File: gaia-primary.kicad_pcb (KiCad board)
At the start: 4 copper layers, 50 x 50 mm, 24 parts, among them J1 4G antenna connector(U.FL), J6 Global Connector Technology S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, Q1 DTC143ZEBTL, Q3 DTC143ZEBTL, Q4 DTC143ZEBTL, U1 SIM7600E-H, U2 Gaia Connector A, U3 Gaia Connector B

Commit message: adding components
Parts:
- removed C18, C51: 1uF, Capacitor_SMD:C_1812_4532Metric
- removed C2, C20, C24, C4: 220uF, Capacitor_SMD:CP_Elec_5x5.9
- removed C3: 100nF, Capacitor_SMD:C_0402_1005Metric
- removed C47: 100nF, Capacitor_SMD:C_0603_1608Metric
- removed C49, C50: NM_NC, Capacitor_SMD:C_0402_1005Metric
- removed D1, D2: LED, LED_SMD:LED_0402_1005Metric
- removed J1: 4G antenna connector(U.FL), Connector_Coaxial:U.FL_Hirose_U.FL-R-SMT-1_Vertical
- removed J6: Global Connector Technology SIM8060-6-0-14-00-A, Connector_Card:nanoSIM_GCT_SIM8060-6-0-14-00
- removed Q1, Q3, Q4: DTC143ZEBTL, gaia-4gmodul-footprints:DTC143ZEBTL
- removed R19: 0, Resistor_SMD:R_0402_1005Metric
- removed R20: 0, Resistor_SMD:R_0603_1608Metric
- added C10: 10nF, Capacitor_SMD:C_0603_1608Metric, F.Cu at (130.0, 64.9)
- added C11: 100nF, Capacitor_SMD:C_0603_1608Metric, F.Cu at (130.0, 67.4)
- added C12: 100nF, Capacitor_SMD:C_0603_1608Metric, F.Cu at (130.0, 69.9)
- added C13: 10nF, Capacitor_SMD:C_0603_1608Metric, F.Cu at (130.0, 72.4)
- added C8: 100nF, Capacitor_SMD:C_0603_1608Metric, F.Cu at (130.0, 59.8)
- added C9: 100nF, Capacitor_SMD:C_0603_1608Metric, F.Cu at (130.0, 62.4)
- added U4: STM32F103C8Tx, Package_QFP:LQFP-48_7x7mm_P0.5mm, F.Cu at (189.4, 107.9)
- added U5: ICM-20948, Sensor_Motion:InvenSense_QFN-24_3x3mm_P0.4mm, F.Cu at (196.1, 75.0)
- added U6: BME680/BME690, Package_LGA:Bosch_LGA-8_3x3mm_P0.8mm_ClockwisePinNumbering, F.Cu at (207.2, 74.0)
- added U7: ICM-20948, Sensor_Motion:InvenSense_QFN-24_3x3mm_P0.4mm, F.Cu at (181.7, 75.1)
- added U8: MAX31865xTP, Package_DFN_QFN:TQFN-20-1EP_5x5mm_P0.65mm_EP3.1x3.1mm, F.Cu at (200.1, 103.5)
- added U9: MAX31865xTP, Package_DFN_QFN:TQFN-20-1EP_5x5mm_P0.65mm_EP3.1x3.1mm, F.Cu at (179.0, 103.5)
- R12, R13: value 750 -> 4kOhm 0,1%; footprint Resistor_SMD:R_0402_1005Metric -> Resistor_SMD:R_1206_3216Metric
- U1: value SIM7600E-H -> BME680/BME690; footprint gaia-4gmodul-footprints:SIM7600 -> Package_LGA:Bosch_LGA-8_3x3mm_P0.8mm_ClockwisePinNumbering
- moved R13 76.9 mm to (134.8, 78.1)
- moved R12 73.4 mm to (134.8, 74.7)
- moved U1 25.2 mm to (171.3, 73.8)
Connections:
- U1 pad 2: GND -> unconnected-(U1-CSB-Pad2)
- U1 pad 3: Net-(U1-PWRKEY) -> unconnected-(U1-SDI-Pad3)
- U1 pad 4: /reset -> unconnected-(U1-SCK-Pad4)
- U1 pad 5: GND -> unconnected-(U1-SDO-Pad5)
- U1 pad 7: unconnected-(U1-SPI_MISO-Pad7) -> GND
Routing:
- net GND: track 117.2 -> 0.71 mm, vias 28 -> 0
- net /Vbat: track 46.8 -> 0.00 mm, vias 9 -> 0
- net /status: track 20.2 -> 0.00 mm
- net /netlight: track 16.8 -> 0.00 mm
- net /reset: track 12.7 -> 0.00 mm
- net /USIM_DATA: track 10.9 -> 0.00 mm, vias 1 -> 0
- net /USIM_CLK: track 10.0 -> 0.00 mm, vias 1 -> 0
- net Net-(U1-PWRKEY): track 7.16 -> 0.00 mm, vias 1 -> 0
- net /USIM_RESET: track 6.47 -> 0.00 mm, vias 1 -> 0
- net /USIM_VDD: track 5.93 -> 0.00 mm, vias 1 -> 0
- net Net-(U1-MAIN_ANT): track 4.21 -> 0.00 mm
- net Net-(J1-In): track 2.50 -> 0.00 mm
- net Net-(U8-BIAS): track 1.87 -> 0.00 mm
- net Net-(U9-BIAS): track 1.87 -> 0.00 mm
- net Net-(U9-ISENSOR): track 1.30 -> 0.00 mm
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- added copper zone on In2.Cu, net (none)
- removed copper zone on In2.Cu, net /Vbat
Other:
- outline, holes or cut-outs redrawn
- board text removed: "NET"
- board text removed: "STATUS"

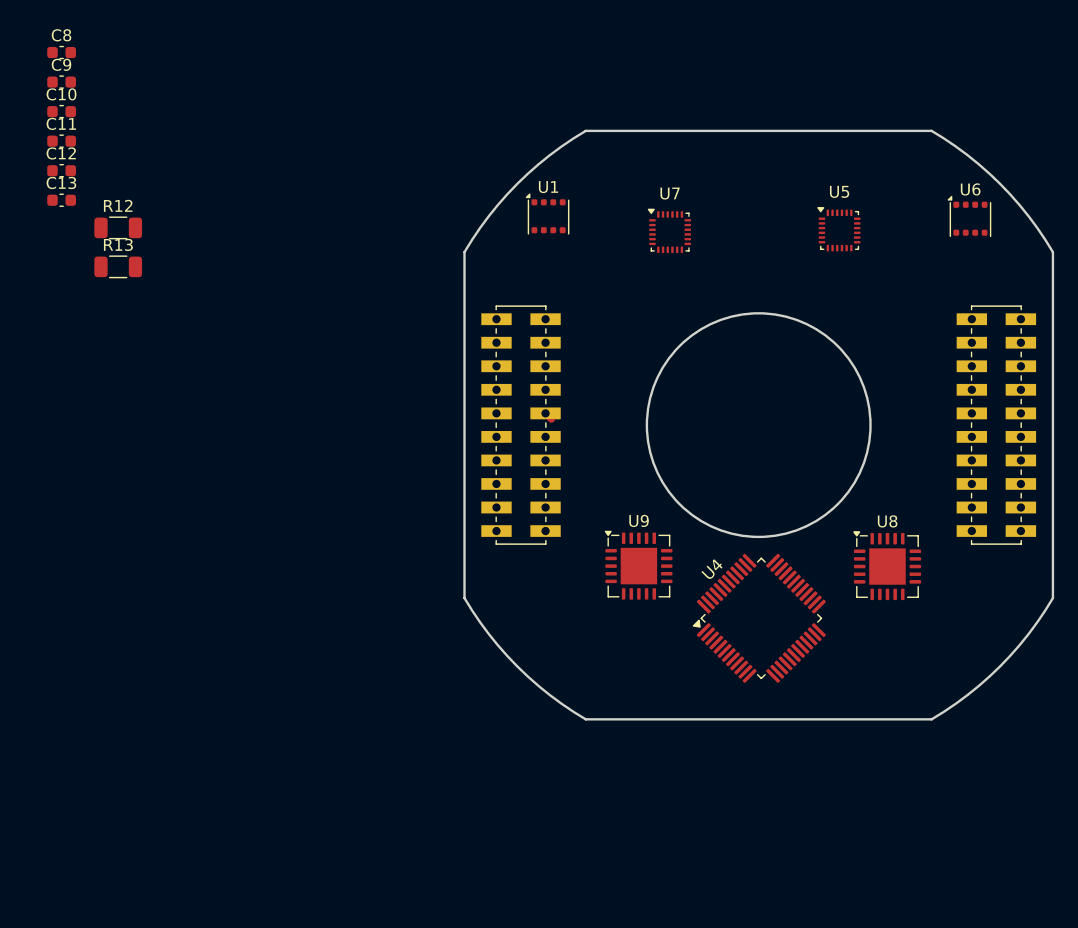
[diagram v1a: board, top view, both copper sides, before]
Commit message: Adding ADI ADXL375 + Creating hierarchical sheets
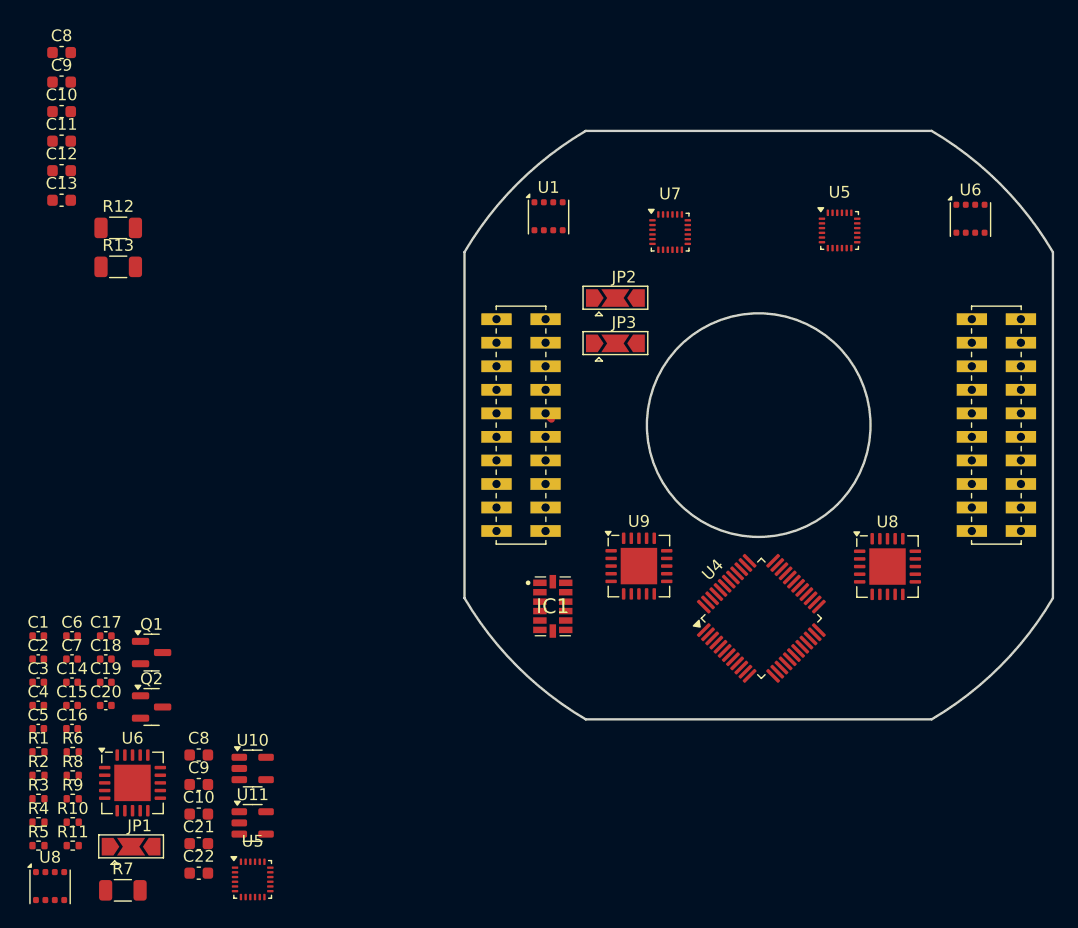
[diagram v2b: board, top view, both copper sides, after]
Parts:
- added C1: 1uF, Capacitor_SMD:C_0402_1005Metric, F.Cu at (128.0, 109.4)
- added C10: 10nF, Capacitor_SMD:C_0603_1608Metric, F.Cu at (141.6, 124.5)
- added C14: 100nF, Capacitor_SMD:C_0402_1005Metric, F.Cu at (130.8, 113.3)
- added C15: 100nF, Capacitor_SMD:C_0402_1005Metric, F.Cu at (130.8, 115.3)
- added C16: 100nF, Capacitor_SMD:C_0402_1005Metric, F.Cu at (130.8, 117.3)
- added C17: 100nF, Capacitor_SMD:C_0402_1005Metric, F.Cu at (133.7, 109.4)
- added C18: 100nF, Capacitor_SMD:C_0402_1005Metric, F.Cu at (133.7, 111.4)
- added C19: 100nF, Capacitor_SMD:C_0402_1005Metric, F.Cu at (133.7, 113.3)
- added C2: 1uF, Capacitor_SMD:C_0402_1005Metric, F.Cu at (128.0, 111.4)
- added C20: 100nF, Capacitor_SMD:C_0402_1005Metric, F.Cu at (133.7, 115.3)
- added C21: 100nF, Capacitor_SMD:C_0603_1608Metric, F.Cu at (141.6, 127.1)
- added C22: 100nF, Capacitor_SMD:C_0603_1608Metric, F.Cu at (141.6, 129.6)
- added C3: 1uF, Capacitor_SMD:C_0402_1005Metric, F.Cu at (128.0, 113.3)
- added C4: 1uF, Capacitor_SMD:C_0402_1005Metric, F.Cu at (128.0, 115.3)
- added C5: 100nF, Capacitor_SMD:C_0402_1005Metric, F.Cu at (128.0, 117.3)
- added C6: 100nF, Capacitor_SMD:C_0402_1005Metric, F.Cu at (130.8, 109.4)
- added C7: 100nF, Capacitor_SMD:C_0402_1005Metric, F.Cu at (130.8, 111.4)
- added C8: 100nF, Capacitor_SMD:C_0603_1608Metric, F.Cu at (141.6, 119.5)
- added C9: 100nF, Capacitor_SMD:C_0603_1608Metric, F.Cu at (141.6, 122.0)
- added IC1: ADXL375BCCZ, gaia-primary-footprints:CC-14-1, F.Cu at (171.7, 106.9)
- added JP1: SolderJumper_3_Open, Jumper:SolderJumper-3_P2.0mm_Open_TrianglePad1.0x1.5mm, F.Cu at (135.9, 127.3)
- added JP2: SolderJumper_3_Open, Jumper:SolderJumper-3_P2.0mm_Open_TrianglePad1.0x1.5mm, F.Cu at (177.0, 80.7)
- added JP3: SolderJumper_3_Open, Jumper:SolderJumper-3_P2.0mm_Open_TrianglePad1.0x1.5mm, F.Cu at (177.0, 84.6)
- added Q1: BSS138, Package_TO_SOT_SMD:SOT-23, F.Cu at (137.6, 110.8)
- added Q2: BSS138, Package_TO_SOT_SMD:SOT-23, F.Cu at (137.6, 115.5)
- added R1: 10k, Resistor_SMD:R_0402_1005Metric, F.Cu at (128.0, 119.3)
- added R10: 10k, Resistor_SMD:R_0402_1005Metric, F.Cu at (130.9, 125.2)
- added R11: 10k, Resistor_SMD:R_0402_1005Metric, F.Cu at (130.9, 127.2)
- added R2: 10k, Resistor_SMD:R_0402_1005Metric, F.Cu at (128.0, 121.3)
- added R3: 10k, Resistor_SMD:R_0402_1005Metric, F.Cu at (128.0, 123.2)
- added R4: 10k, Resistor_SMD:R_0402_1005Metric, F.Cu at (128.0, 125.2)
- added R5: 10k, Resistor_SMD:R_0402_1005Metric, F.Cu at (128.0, 127.2)
- added R6: 10k, Resistor_SMD:R_0402_1005Metric, F.Cu at (130.9, 119.3)
- added R7: 4kOhm 0,1%, Resistor_SMD:R_1206_3216Metric, F.Cu at (135.2, 131.0)
- added R8: 10k, Resistor_SMD:R_0402_1005Metric, F.Cu at (130.9, 121.3)
- added R9: 10k, Resistor_SMD:R_0402_1005Metric, F.Cu at (130.9, 123.2)
- added U10: AP2112K-1.8, Package_TO_SOT_SMD:SOT-23-5, F.Cu at (146.2, 120.7)
- added U11: AP2112K-3.3, Package_TO_SOT_SMD:SOT-23-5, F.Cu at (146.2, 125.3)
- added U5: ICM-20948, Sensor_Motion:InvenSense_QFN-24_3x3mm_P0.4mm, F.Cu at (146.2, 130.1)
- added U6: MAX31865xTP, Package_DFN_QFN:TQFN-20-1EP_5x5mm_P0.65mm_EP3.1x3.1mm, F.Cu at (136.0, 121.9)
- added U8: BME680/BME690, Package_LGA:Bosch_LGA-8_3x3mm_P0.8mm_ClockwisePinNumbering, F.Cu at (129.0, 130.7)
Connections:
- net CS2 renamed /LOCAL_CS_2
- U1 pad 2: unconnected-(U1-CSB-Pad2) -> +3.3V
- U1 pad 3: unconnected-(U1-SDI-Pad3) -> /LOCAL_SDA
- U1 pad 4: unconnected-(U1-SCK-Pad4) -> /LOCAL_SCL
- U1 pad 5: unconnected-(U1-SDO-Pad5) -> GND
- U1 pad 6: unconnected-(U1-VDDIO-Pad6) -> +3.3V
- U1 pad 8: unconnected-(U1-VDD-Pad8) -> +3.3V
- U2 pad 10: /VOUT_B2 -> unconnected-(U2-VOUT_B2-Pad10)
- U2 pad 3: /VOUT_A2 -> unconnected-(U2-VOUT_A2-Pad3)
- U2 pad 4: /VOUT_A2 -> unconnected-(U2-VOUT_A2-Pad4)
- U2 pad 5: /VOUT_A3 -> unconnected-(U2-VOUT_A3-Pad5)
- U2 pad 6: /VOUT_A3 -> unconnected-(U2-VOUT_A3-Pad6)
- U2 pad 9: /VOUT_B2 -> unconnected-(U2-VOUT_B2-Pad9)
- U7 pad 10: unconnected-(U7-REGOUT-Pad10) -> Net-(U7-REGOUT)
- U7 pad 13: unconnected-(U7-VDD-Pad13) -> +1V8
- U7 pad 18: Net-(U7-GND-Pad18) -> GND
- U7 pad 20: Net-(U7-GND-Pad18) -> GND
- U7 pad 23: unconnected-(U7-SCL/SCLK-Pad23) -> /SCL_1V8
- U7 pad 24: unconnected-(U7-SDA/SDI-Pad24) -> /SDA_1V8
- U7 pad 8: unconnected-(U7-VDDIO-Pad8) -> +1V8
- U7 pad 9: unconnected-(U7-SDO/AD0-Pad9) -> +1V8
- U9 pad 11: SDI -> /LOCAL_MOSI
- U9 pad 12: SCLK -> /LOCAL_SCLK
- U9 pad 14: SDO -> /LOCAL_MISO
- U9 pad 18: DRDY -> /LOCAL_RD_2

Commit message: Finalizing PCB, routing
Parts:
- removed the C10 at (130.0, 64.9)
- removed the C10 at (141.6, 124.5)
- removed C21, C22: 100nF, Capacitor_SMD:C_0603_1608Metric
- removed the C8 at (130.0, 59.8)
- removed the C8 at (141.6, 119.5)
- removed the C9 at (141.6, 122.0)
- removed the C9 at (130.0, 62.4)
- removed IC1: ADXL375BCCZ, gaia-primary-footprints:CC-14-1
- removed U1, U8: BME680/BME690, Package_LGA:Bosch_LGA-8_3x3mm_P0.8mm_ClockwisePinNumbering
- removed U2: Gaia Connector A, gaia-4gmodul-footprints:Gaia_connector_4_6layer
- removed U3: Gaia Connector B, gaia-4gmodul-footprints:Gaia_connector_4_6layer
- removed the U5 at (196.1, 75.0)
- removed the U5 at (146.2, 130.1)
- removed the U6 at (207.2, 74.0)
- removed the U6 at (136.0, 121.9)
- removed U8: MAX31865xTP, Package_DFN_QFN:TQFN-20-1EP_5x5mm_P0.65mm_EP3.1x3.1mm
- added C10: 100nF, Capacitor_SMD:C_0402_1005Metric, F.Cu at (184.0, 115.2)
- added C23: 100nF, Capacitor_SMD:C_0402_1005Metric, F.Cu at (187.8, 75.5)
- added C24: 100nF, Capacitor_SMD:C_0402_1005Metric, F.Cu at (191.1, 75.5)
- added C25: 100nF, Capacitor_SMD:C_0402_1005Metric, F.Cu at (195.2, 72.0)
- added C26: 100nF, Capacitor_SMD:C_0402_1005Metric, F.Cu at (197.7, 75.7)
- added C27: 100nF, Capacitor_SMD:C_0402_1005Metric, F.Cu at (194.8, 73.4)
- added C28: 100nF, Capacitor_SMD:C_0402_1005Metric, F.Cu at (207.4, 74.5)
- added C29: 100nF, Capacitor_SMD:C_0402_1005Metric, F.Cu at (204.8, 70.7)
- added C30: 100nF, Capacitor_SMD:C_0402_1005Metric, F.Cu at (207.8, 72.7)
- added C8: 100nF, Capacitor_SMD:C_0402_1005Metric, F.Cu at (185.9, 115.2)
- added C9: 100nF, Capacitor_SMD:C_0402_1005Metric, F.Cu at (192.8, 115.2)
- added D1: LED_Small, LED_SMD:LED_0603_1608Metric, F.Cu at (182.5, 69.0)
- added IC2: ADXL375BCCZ, gaia-primary-footprints:CC-14-1, F.Cu at (189.4, 72.9)
- added J1: Debug Connectors, gaia-primary-footprints:PinHeader_1x07_P2.54mm_Vertical, F.Cu at (181.6, 107.8)
- added J2: Conn_02x10_Odd_Even, gaia-primary-footprints:Gaia_connector_2_4layer, F.Cu at (169.0, 91.5)
- added J3: Conn_02x10_Odd_Even, gaia-primary-footprints:Gaia_connector_2_4layer, F.Cu at (209.4, 91.5)
- added R14: 10k, Resistor_SMD:R_0402_1005Metric, F.Cu at (187.4, 69.9)
- added R15: 10k, Resistor_SMD:R_0402_1005Metric, F.Cu at (196.9, 112.2)
- added R16: 10k, Resistor_SMD:R_0402_1005Metric, F.Cu at (188.2, 112.2)
- added TH3: Pt1000, gaia-primary-footprints:yageo_m1020, F.Cu at (178.0, 115.5)
- added TH4: Pt1000, gaia-primary-footprints:yageo_m1020, F.Cu at (200.3, 115.5)
- added U12: ICM-20948, gaia-primary-footprints:InvenSense_QFN-24_3x3mm_P0.4mm, F.Cu at (197.7, 73.2)
- added U13: ICM-20948, gaia-primary-footprints:InvenSense_QFN-24_3x3mm_P0.4mm, F.Cu at (204.8, 73.2)
- added U5: MAX31865xTP, gaia-primary-footprints:TQFN-20-1EP_5x5mm_P0.65mm_EP3.1x3.1mm, F.Cu at (175.2, 107.8)
- added U6: BME680/BME690, gaia-primary-footprints:Bosch_LGA-8_3x3mm_P0.8mm_ClockwisePinNumbering, F.Cu at (185.0, 113.0)
- added Y1: Crystal, gaia-primary-footprints:NX3225GD8MHZSTDCRA3, B.Cu at (175.8, 78.3)
- C1, C2, C3, C4, R1, R2, R3, R4: moved to B.Cu
- C11: footprint Capacitor_SMD:C_0603_1608Metric -> Capacitor_SMD:C_0402_1005Metric
- C12: value 100nF -> 22pF; footprint Capacitor_SMD:C_0603_1608Metric -> Capacitor_SMD:C_0402_1005Metric; moved to B.Cu
- C13: value 10nF -> 22pF; footprint Capacitor_SMD:C_0603_1608Metric -> Capacitor_SMD:C_0402_1005Metric; moved to B.Cu
- C16, C7: value 100nF -> 10nF
- JP1, JP2, JP3: footprint Jumper:SolderJumper-3_P2.0mm_Open_TrianglePad1.0x1.5mm -> gaia-primary-footprints:SolderJumper-3_P2.0mm_Open_TrianglePad1.0x1.5mm; moved to B.Cu
- Q1, Q2: footprint Package_TO_SOT_SMD:SOT-23 -> gaia-primary-footprints:SOT-23; moved to B.Cu
- R10, R11: value 10k -> 4kOhm 0,1%; footprint Resistor_SMD:R_0402_1005Metric -> Resistor_SMD:R_1206_3216Metric
- R12, R13, R7: value 4kOhm 0,1% -> 10k; footprint Resistor_SMD:R_1206_3216Metric -> Resistor_SMD:R_0402_1005Metric
- R5: value 10k -> 100
- R6: value 10k -> TBA
- U10, U11: footprint Package_TO_SOT_SMD:SOT-23-5 -> gaia-primary-footprints:SOT-23-5; moved to B.Cu
- U4: footprint Package_QFP:LQFP-48_7x7mm_P0.5mm -> gaia-primary-footprints:LQFP-48_7x7mm_P0.5mm
- U7: value ICM-20948 -> MAX31865xTP; footprint Sensor_Motion:InvenSense_QFN-24_3x3mm_P0.4mm -> gaia-primary-footprints:TQFN-20-1EP_5x5mm_P0.65mm_EP3.1x3.1mm
- U9: value MAX31865xTP -> BME680/BME690; footprint Package_DFN_QFN:TQFN-20-1EP_5x5mm_P0.65mm_EP3.1x3.1mm -> gaia-primary-footprints:Bosch_LGA-8_3x3mm_P0.8mm_ClockwisePinNumbering
- moved R2 91.7 mm to (203.4, 69.2), turned to -90 degrees
- moved R4 90.1 mm to (201.6, 73.3), turned to -90 degrees
- moved C4 88.8 mm to (205.7, 72.5)
- moved C2 88.6 mm to (207.6, 72.5), turned to 180 degrees
- moved JP1 86.8 mm to (208.3, 79.5), turned to 180 degrees
- moved R3 86.4 mm to (197.8, 72.3), turned to -90 degrees
- moved R1 86.2 mm to (199.6, 71.2), turned to 90 degrees
- moved C1 86.0 mm to (207.9, 77.6), turned to 180 degrees
- moved C3 84.4 mm to (204.4, 77.6), turned to 180 degrees
- moved C11 80.4 mm to (194.6, 115.2), turned to 180 degrees
- moved U11 79.2 mm to (207.4, 75.0), turned to 90 degrees
- moved Q1 75.9 mm to (202.0, 70.6)
- moved C15 74.5 mm to (204.4, 103.8), turned to 90 degrees
- moved Q2 74.3 mm to (199.2, 73.8), turned to 180 degrees
- moved C16 74.0 mm to (204.6, 111.4)
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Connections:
- C12 pad 1: +3.3V -> Net-(C12-Pad1)
- C13 pad 1: Net-(U9-FORCE+) -> GND
- C13 pad 2: Net-(U9-FORCE-) -> Net-(U4-PD0)
- C14 pad 2: +1V8 -> +3.3V
- C15 pad 1: GND -> +3.3V
- C15 pad 2: +1V8 -> GND
- C16 pad 1: GND -> Net-(U7-FORCE+)
- C16 pad 2: Net-(U5-REGOUT) -> Net-(U7-FORCE-)
- C17 pad 1: GND -> +3.3V
- C17 pad 2: +3.3V -> GND
- C18 pad 1: GND -> +3.3V
- C18 pad 2: +3.3V -> GND
- C19 pad 1: GND -> +3.3V
- C19 pad 2: +3.3V -> GND
- C20 pad 1: GND -> +3.3V
- C20 pad 2: +3.3V -> GND
- C5 pad 2: +1V8 -> +3.3V
- C6 pad 1: GND -> +3.3V
- C6 pad 2: +1V8 -> GND
- C7 pad 1: GND -> Net-(U5-FORCE+)
- C7 pad 2: Net-(U7-REGOUT) -> Net-(U5-FORCE-)
- JP2 pad 2: /LOCAL_SCL -> /GLOBAL_SCL
- JP3 pad 2: /LOCAL_SDA -> /GLOBAL_SDA
- R10 pad 1: +3.3V -> Net-(U5-BIAS)
- R10 pad 2: /LOCAL_SCL -> Net-(U5-ISENSOR)
- R11 pad 1: +3.3V -> Net-(U7-BIAS)
- R11 pad 2: /LOCAL_SDA -> Net-(U7-ISENSOR)
- R12 pad 1: Net-(U8-BIAS) -> +3.3V
- R12 pad 2: Net-(U8-ISENSOR) -> /LOCAL_SCL
- R13 pad 1: Net-(U9-BIAS) -> +3.3V
- R13 pad 2: Net-(U9-ISENSOR) -> /LOCAL_SCL
- R5 pad 1: +3.3V -> Net-(C12-Pad1)
- R5 pad 2: /LOCAL_SCL -> Net-(U4-PD1)
- R6 pad 1: +3.3V -> GND
- R6 pad 2: /LOCAL_SDA -> Net-(D1-K)
- R7 pad 1: Net-(U6-BIAS) -> +3.3V
- R7 pad 2: Net-(U6-ISENSOR) -> /LOCAL_SCL
- R8 pad 1: +3.3V -> GND
- R8 pad 2: /LOCAL_SCL -> Net-(U4-BOOT0)
- R9 pad 1: +3.3V -> /DEBUG_NRST
- R9 pad 2: /LOCAL_SDA -> +3.3V
- U4 pad 11: unconnected-(U4-PA1-Pad11) -> /READY1
- U4 pad 12: unconnected-(U4-PA2-Pad12) -> /READY2
- U4 pad 13: unconnected-(U4-PA3-Pad13) -> /SPI1_CS1
- U4 pad 14: unconnected-(U4-PA4-Pad14) -> /SPI1_CS2
- U4 pad 15: unconnected-(U4-PA5-Pad15) -> /SPI1_SCK
- U4 pad 16: unconnected-(U4-PA6-Pad16) -> /SPI1_MISO
- U4 pad 17: unconnected-(U4-PA7-Pad17) -> /SPI1_MOSI
- U4 pad 21: unconnected-(U4-PB10-Pad21) -> /LOCAL_SCL
- U4 pad 22: unconnected-(U4-PB11-Pad22) -> /LOCAL_SDA
- U4 pad 23: Net-(U4-VSS-Pad23) -> GND
- U4 pad 24: unconnected-(U4-VDD-Pad24) -> +3.3V
- U4 pad 25: unconnected-(U4-PB12-Pad25) -> Net-(D1-A)
- U4 pad 30: unconnected-(U4-PA9-Pad30) -> /DEBUG_USART_TX
- U4 pad 31: unconnected-(U4-PA10-Pad31) -> /DEBUG_USART_RX
- U4 pad 34: unconnected-(U4-PA13-Pad34) -> /DEBUG_SWD_IO
- U4 pad 35: Net-(U4-VSS-Pad23) -> GND
- U4 pad 36: unconnected-(U4-VDD-Pad36) -> +3.3V
- U4 pad 37: unconnected-(U4-PA14-Pad37) -> /DEBUG_SWD_CLK
- U4 pad 42: unconnected-(U4-PB6-Pad42) -> /GLOBAL_SCL
- U4 pad 43: unconnected-(U4-PB7-Pad43) -> /GLOBAL_SDA
- U4 pad 44: unconnected-(U4-BOOT0-Pad44) -> Net-(U4-BOOT0)
- U4 pad 47: Net-(U4-VSS-Pad23) -> GND
- U4 pad 48: unconnected-(U4-VDD-Pad48) -> +3.3V
- U4 pad 5: unconnected-(U4-PD0-Pad5) -> Net-(U4-PD0)
- U4 pad 6: unconnected-(U4-PD1-Pad6) -> Net-(U4-PD1)
- U4 pad 7: unconnected-(U4-NRST-Pad7) -> /DEBUG_NRST
- U4 pad 8: unconnected-(U4-VSSA-Pad8) -> GND
- U4 pad 9: unconnected-(U4-VDDA-Pad9) -> +3.3V
- U7 pad 1: unconnected-(U7-NC-Pad1) -> Net-(U7-BIAS)
- U7 pad 10: Net-(U7-REGOUT) -> GND
- U7 pad 11: unconnected-(U7-FSYNC-Pad11) -> /SPI1_MOSI
- U7 pad 12: unconnected-(U7-INT1-Pad12) -> /SPI1_SCK
- U7 pad 13: +1V8 -> /SPI1_CS2
- U7 pad 14: unconnected-(U7-NC-Pad14) -> /SPI1_MISO
- U7 pad 15: unconnected-(U7-NC-Pad15) -> GND
- U7 pad 16: unconnected-(U7-NC-Pad16) -> GND
- U7 pad 18: GND -> /READY2
- U7 pad 19: unconnected-(U7-RESV-Pad19) -> +3.3V
- U7 pad 2: unconnected-(U7-NC-Pad2) -> Net-(U7-BIAS)
- U7 pad 20: GND -> +3.3V
- U7 pad 21: unconnected-(U7-AUX_DA-Pad21) -> GND
- U7 pad 3: unconnected-(U7-NC-Pad3) -> Net-(U7-ISENSOR)
- U7 pad 4: unconnected-(U7-NC-Pad4) -> Net-(U7-ISENSOR)
- U7 pad 5: unconnected-(U7-NC-Pad5) -> Net-(U7-FORCE+)
- U7 pad 6: unconnected-(U7-NC-Pad6) -> GND
- U7 pad 7: unconnected-(U7-AUX_CL-Pad7) -> Net-(U7-FORCE+)
- U7 pad 8: +1V8 -> Net-(U7-FORCE-)
- U7 pad 9: +1V8 -> Net-(U7-FORCE-)
- U9 pad 1: Net-(U9-BIAS) -> GND
- U9 pad 2: Net-(U9-BIAS) -> +3.3V
- U9 pad 3: Net-(U9-ISENSOR) -> /LOCAL_SDA
- U9 pad 4: Net-(U9-ISENSOR) -> /LOCAL_SCL
- U9 pad 5: Net-(U9-FORCE+) -> +3.3V
- U9 pad 6: GND -> +3.3V
- U9 pad 7: Net-(U9-FORCE+) -> GND
- U9 pad 8: Net-(U9-FORCE-) -> +3.3V
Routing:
- net /LOCAL_SDA: track 0.00 -> 115.5 mm, vias 0 -> 3
- net /LOCAL_SCL: track 0.00 -> 101.9 mm, vias 0 -> 3
- net /SPI1_MOSI: track 0.00 -> 95.4 mm, vias 0 -> 2
- net /SPI1_MISO: track 0.00 -> 89.9 mm, vias 0 -> 3
- net /SPI1_SCK: track 0.00 -> 86.1 mm, vias 0 -> 3
- net GND: track 0.71 -> 86.2 mm, vias 0 -> 33
- net /SPI1_CS1: track 0.00 -> 65.6 mm, vias 0 -> 2
- net /DEBUG_USART_TX: track 0.00 -> 62.5 mm
- net +3.3V: track 0.00 -> 61.1 mm, vias 0 -> 16
- net /DEBUG_NRST: track 0.00 -> 58.3 mm, vias 0 -> 1
- net /SPI1_CS2: track 0.00 -> 56.7 mm, vias 0 -> 4
- net /READY1: track 0.00 -> 51.7 mm, vias 0 -> 2
- net /DEBUG_USART_RX: track 0.00 -> 51.3 mm, vias 0 -> 2
- net /DEBUG_SWD_IO: track 0.00 -> 50.3 mm, vias 0 -> 2
- net /READY2: track 0.00 -> 49.3 mm, vias 0 -> 2
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- added copper zone on In2.Cu, net +3.3V
- removed copper zone on In2.Cu, net (none)
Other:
- outline, holes or cut-outs redrawn
- board text added: "3V3"
- board text added: "A"
- board text added: "B"
- board text added: "CLK"
- board text added: "DIO"
- board text added: "GND"
- board text added: "Primary Mission"
- board text added: "RST"
- board text added: "RX"
- board text added: "TX"
- board text added: "revision 1.0 Designed by Tamás Pécsi"

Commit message: Update gaia-primary.kicad_pcb
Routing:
- net /SPI1_MOSI: track 95.4 -> 96.5 mm
